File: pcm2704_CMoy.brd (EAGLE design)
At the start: 100.3 x 77.5 mm, 84 parts, among them IC3 7815DT, IC4 tsr 1-2433, IC5 7915TV, Q1 12MHz, U1 PCM2704, U2 OPA2134P, U3 TC962EPA, X2 PN61729-S, X5 22-23-2031, X6 22-23-2031

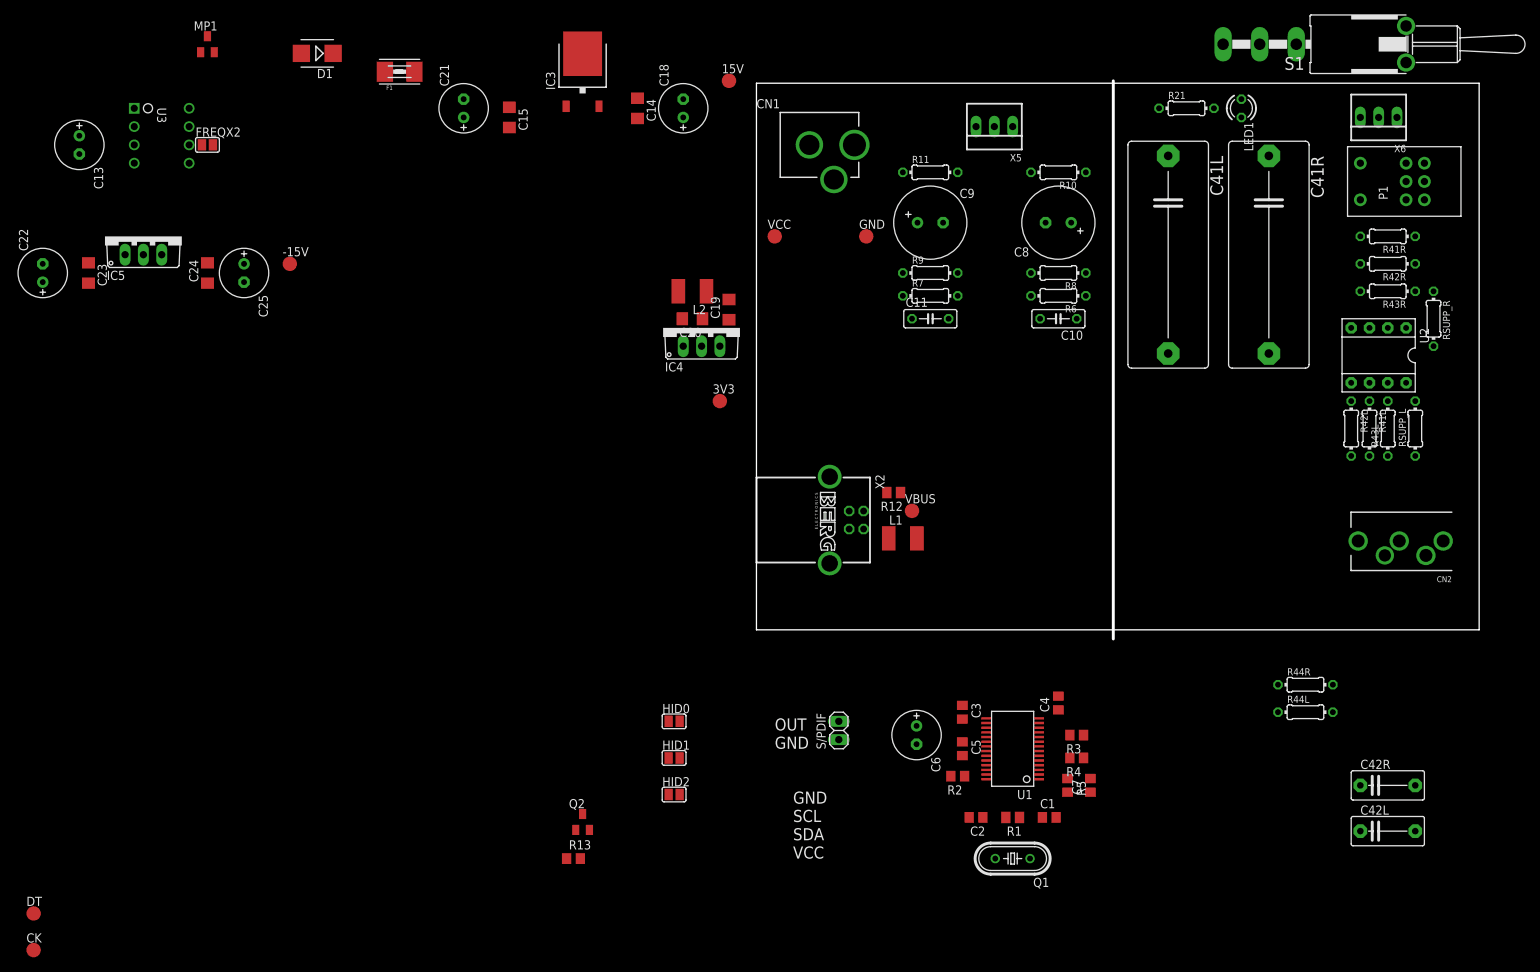
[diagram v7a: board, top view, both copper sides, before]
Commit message: - Cosmetics
 - Added bus power indicator led
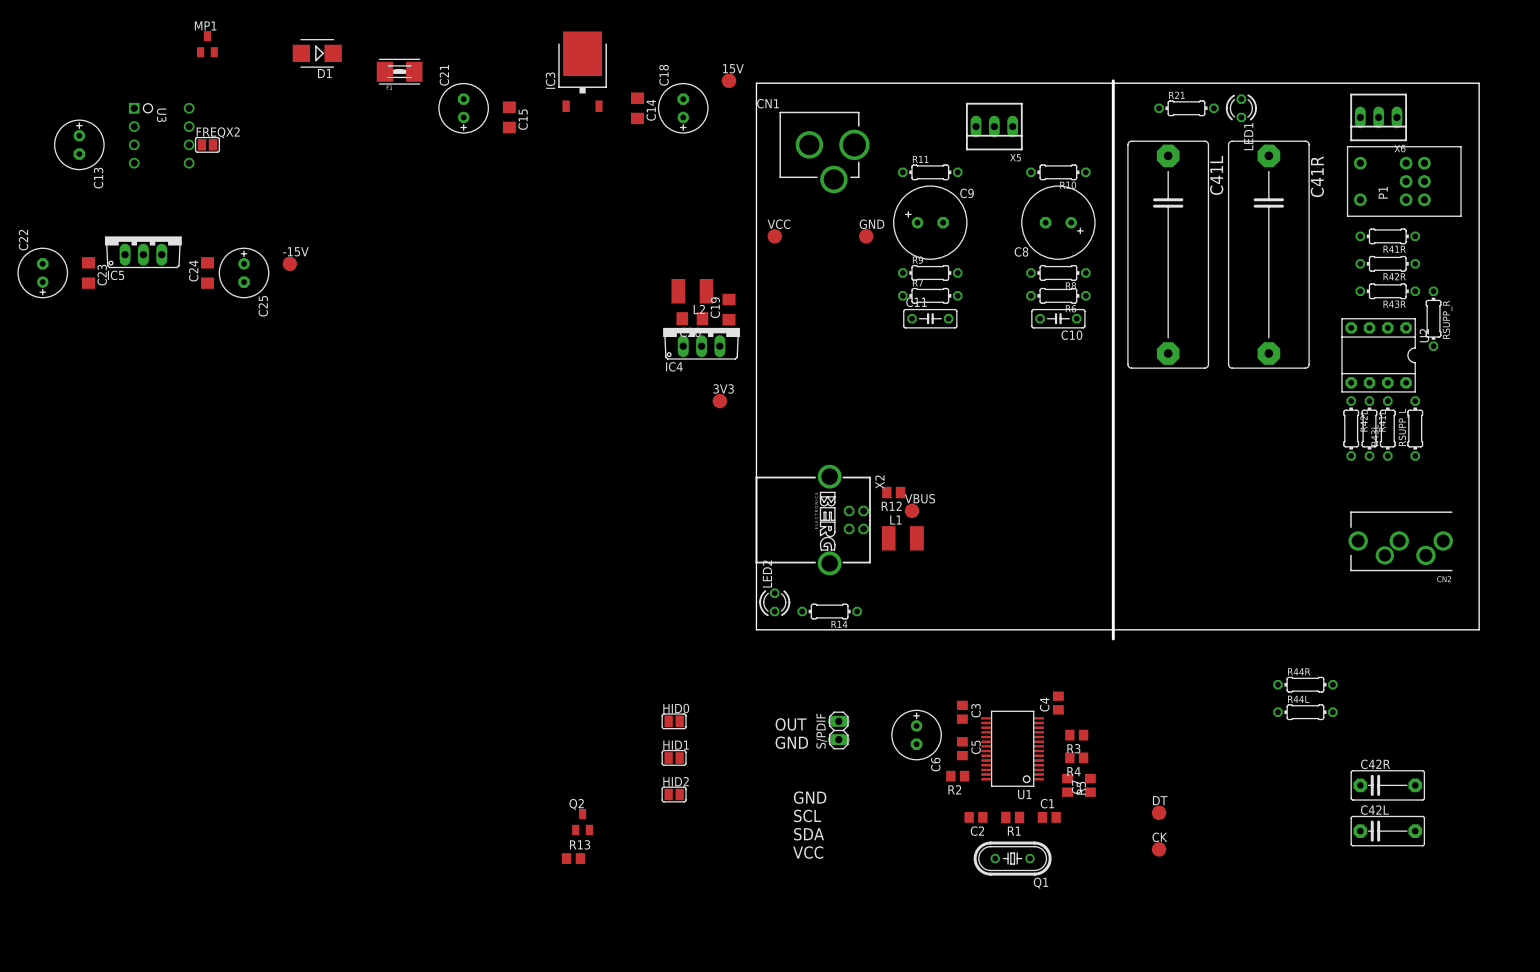
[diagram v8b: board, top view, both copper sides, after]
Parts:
- removed S1: (no value), switch:LPV-1
- added LED2: (no value), led:LED3MM
- added R14: 470R, rcl:0204/7
- moved CK 156.8 mm to (55.9, -30.5)
- moved DT 156.8 mm to (55.9, -25.4)
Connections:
- new net N$2: LED2.A, R14.2
- net GND: now also LED2.K
- net VBUS: now also R14.1
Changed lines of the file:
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@@
 <element name="C25" library="rcl" package="E2,5-7" value="100uF" x="-71.12" y="49.53" rot="R270"/>
 <element name="FREQX2" library="jumper" package="SJ" value="" x="-76.2" y="67.31"/>
-<element name="S1" library="switch" package="LPV-1" value="" x="90.17" y="81.28" rot="R90"/>
 <element name="R44R" library="rcl" package="0204/7" value="" x="76.2" y="-7.62"/>
 <element name="R44L" library="rcl" package="0204/7" value="" x="76.2" y="-11.43"/>
@@
 <element name="Q2" library="semicon-smd-ipc" package="SOT23" value="" x="-24.13" y="-26.67"/>
 <element name="R13" library="rcl" package="R0805" value="10K" x="-25.4" y="-31.75"/>
-<element name="DT" library="testpad" package="TP20R" value="TPTP20R" x="-100.33" y="-39.37"/>
-<element name="CK" library="testpad" package="TP20R" value="TPTP20R" x="-100.33" y="-44.45"/>
+<element name="DT" library="testpad" package="TP20R" value="TPTP20R" x="55.88" y="-25.4"/>
+<element name="CK" library="testpad" package="TP20R" value="TPTP20R" x="55.88" y="-30.48"/>
+<element name="LED2" library="led" package="LED3MM" value="" x="2.54" y="3.81" rot="R90"/>
+<element name="R14" library="rcl" package="0204/7" value="470R" x="10.16" y="2.54" rot="R180"/>
 </elements>
 <signals>
@@
 <contactref element="X2" pad="1"/>
 <contactref element="R12" pad="2"/>
-<wire x1="31.904" y1="-16.185" x2="-26.35" y2="-31.75" width="0" layer="19" extent="1-1"/>
-<wire x1="21.59" y1="16.51" x2="31.904" y2="-16.185" width="0" layer="19" extent="1-1"/>
-<wire x1="18.1" y1="19.05" x2="21.59" y2="16.51" width="0" layer="19" extent="1-1"/>
-<wire x1="14.87" y1="13.99" x2="18.1" y2="19.05" width="0" layer="19" extent="1-1"/>
+<contactref element="R14" pad="1"/>
+<wire x1="13.97" y1="2.54" x2="-26.35" y2="-31.75" width="0" layer="19" extent="1-1"/>
+<wire x1="14.87" y1="13.99" x2="13.97" y2="2.54" width="0" layer="19" extent="1-1"/>
+<wire x1="18.1" y1="19.05" x2="14.87" y2="13.99" width="0" layer="19" extent="1-1"/>
+<wire x1="21.59" y1="16.51" x2="18.1" y2="19.05" width="0" layer="19" extent="1-1"/>
+<wire x1="31.904" y1="-16.185" x2="13.97" y2="2.54" width="0" layer="19" extent="1-1"/>
 </signal>
 <signal name="GND">
@@
 <contactref element="HID0" pad="2"/>
 <contactref element="R12" pad="1"/>
+<contactref element="LED2" pad="K"/>
 <wire x1="90.17" y1="64.77" x2="86.36" y2="71.12" width="0" layer="19" extent="1-1"/>
 <wire x1="92.71" y1="64.77" x2="90.17" y2="64.77" width="0" layer="19" extent="1-1"/>
@@
 <wire x1="12.87" y1="13.99" x2="10.16" y2="21.26" width="0" layer="19" extent="1-1"/>
 <wire x1="10.16" y1="9.22" x2="12.87" y2="13.99" width="0" layer="19" extent="1-1"/>
+<wire x1="2.54" y1="5.08" x2="10.16" y2="9.22" width="0" layer="19" extent="1-1"/>
 <wire x1="20" y1="19.05" x2="12.87" y2="13.99" width="0" layer="19" extent="1-1"/>
-<wire x1="11.43" y1="-12.7" x2="10.16" y2="9.22" width="0" layer="19" extent="1-1"/>
+<wire x1="11.43" y1="-12.7" x2="2.54" y2="5.08" width="0" layer="19" extent="1-1"/>
 <wire x1="22.225" y1="-15.875" x2="11.43" y2="-12.7" width="0" layer="19" extent="1-1"/>
 <wire x1="28.575" y1="-15.56" x2="22.225" y2="-15.875" width="0" layer="19" extent="1-1"/>
@@
 <contactref element="U1" pad="3"/>
 <contactref element="DT" pad="TP"/>
-<wire x1="39.216" y1="-19.435" x2="-100.33" y2="-39.37" width="0" layer="19" extent="1-1"/>
-<wire x1="43.18" y1="-22.54" x2="39.216" y2="-19.435" width="0" layer="19" extent="1-1"/>
+<wire x1="43.18" y1="-22.54" x2="55.88" y2="-25.4" width="0" layer="19" extent="1-1"/>
+<wire x1="39.216" y1="-19.435" x2="43.18" y2="-22.54" width="0" layer="19" extent="1-1"/>
 </signal>
 <signal name="N$26">
@@
 <contactref element="U1" pad="2"/>
 <contactref element="CK" pad="TP"/>
-<wire x1="39.216" y1="-20.085" x2="-100.33" y2="-44.45" width="0" layer="19" extent="1-1"/>
+<wire x1="39.216" y1="-20.085" x2="55.88" y2="-30.48" width="0" layer="19" extent="1-1"/>
 </signal>
 <signal name="N$12">
@@
 <wire x1="26.99" y1="-20.32" x2="-23.18" y2="-27.77" width="0" layer="19" extent="1-1"/>
 </signal>
+<signal name="N$2">
+<contactref element="R14" pad="2"/>
+<contactref element="LED2" pad="A"/>
+<wire x1="2.54" y1="2.54" x2="6.35" y2="2.54" width="0" layer="19" extent="1-1"/>
+</signal>
 </signals>
